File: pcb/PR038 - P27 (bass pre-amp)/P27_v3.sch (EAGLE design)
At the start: 51 parts, among them IC1 NE5532P, Q1 BC337

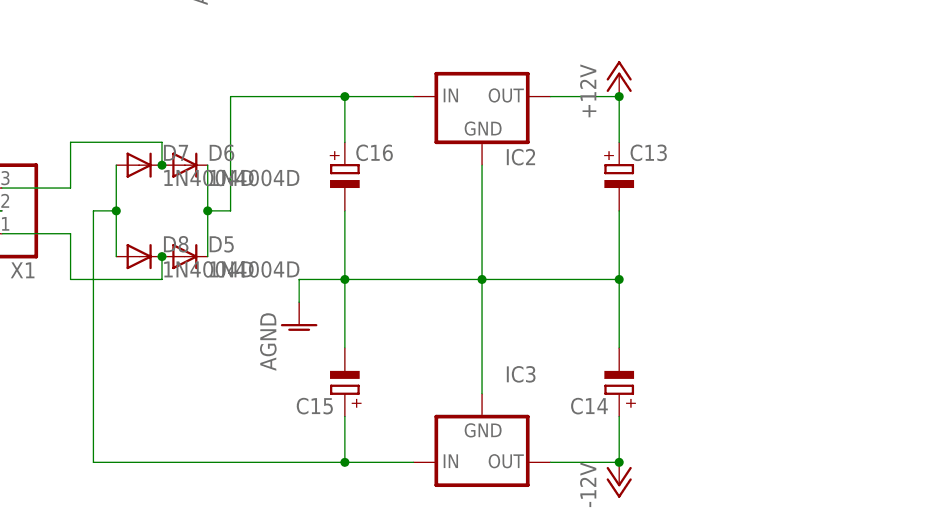
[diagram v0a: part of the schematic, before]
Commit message: 
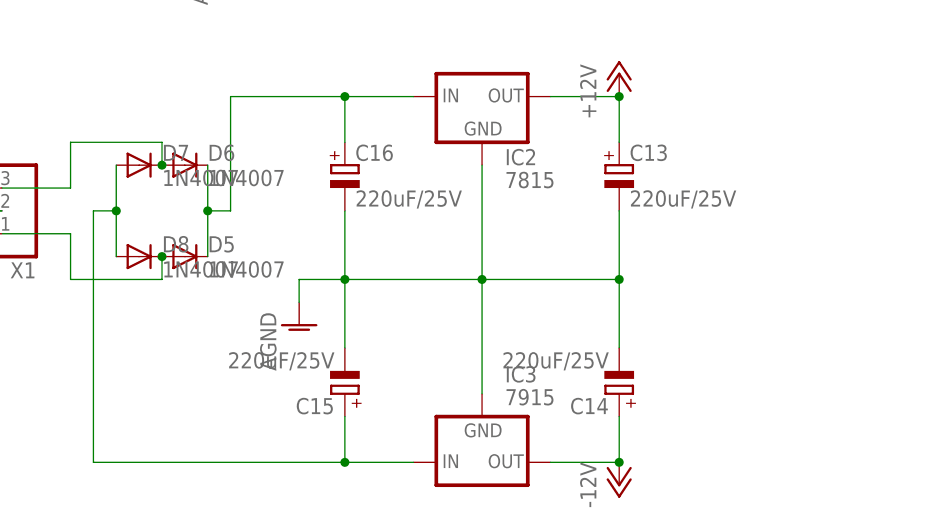
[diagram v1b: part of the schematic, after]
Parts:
- C13, C14, C15, C16: value (none) -> 220uF/25V
- D5, D6, D7, D8: value 1N4004D -> 1N4007
- IC2: value (none) -> 7815
- IC3: value (none) -> 7915
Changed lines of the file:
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@@
 <?xml version="1.0" encoding="utf-8"?>
 <!DOCTYPE eagle SYSTEM "eagle.dtd">
-<eagle version="6.4">
+<eagle version="6.5.0">
 <drawing>
 <settings>
@@
 <part name="X1" library="P27" deviceset="W237-103" device=""/>
 <part name="AGND10" library="P27" deviceset="AGND" device=""/>
-<part name="IC2" library="P27" deviceset="78XX" device="TO-220"/>
-<part name="C13" library="P27" deviceset="CPOL-EU" device="E2.5-6"/>
-<part name="C14" library="P27" deviceset="CPOL-EU" device="E2.5-6"/>
-<part name="C15" library="P27" deviceset="CPOL-EU" device="E2.5-6"/>
-<part name="C16" library="P27" deviceset="CPOL-EU" device="E2.5-6"/>
+<part name="IC2" library="P27" deviceset="78XX" device="TO-220" value="7815"/>
+<part name="C13" library="P27" deviceset="CPOL-EU" device="E2.5-6" value="220uF/25V"/>
+<part name="C14" library="P27" deviceset="CPOL-EU" device="E2.5-6" value="220uF/25V"/>
+<part name="C15" library="P27" deviceset="CPOL-EU" device="E2.5-6" value="220uF/25V"/>
+<part name="C16" library="P27" deviceset="CPOL-EU" device="E2.5-6" value="220uF/25V"/>
 <part name="AGND11" library="P27" deviceset="AGND" device=""/>
 <part name="P+3" library="P27" deviceset="+12V" device=""/>
 <part name="P-3" library="P27" deviceset="-12V" device=""/>
-<part name="IC3" library="P27" deviceset="79XX" device="TO-220"/>
+<part name="IC3" library="P27" deviceset="79XX" device="TO-220" value="7915"/>
 <part name="Q1" library="P27" deviceset="BC337" device=""/>
-<part name="D5" library="P27" deviceset="1N4004" device="D"/>
-<part name="D6" library="P27" deviceset="1N4004" device="D"/>
-<part name="D7" library="P27" deviceset="1N4004" device="D"/>
-<part name="D8" library="P27" deviceset="1N4004" device="D"/>
+<part name="D5" library="P27" deviceset="1N4004" device="D" value="1N4007"/>
+<part name="D6" library="P27" deviceset="1N4004" device="D" value="1N4007"/>
+<part name="D7" library="P27" deviceset="1N4004" device="D" value="1N4007"/>
+<part name="D8" library="P27" deviceset="1N4004" device="D" value="1N4007"/>
 </parts>
 <sheets>

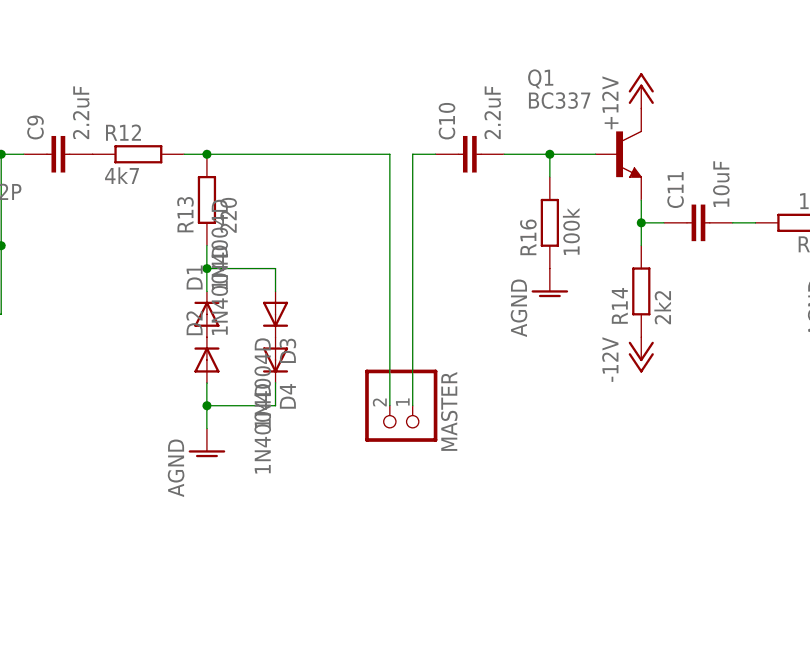
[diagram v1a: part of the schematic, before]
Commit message: 
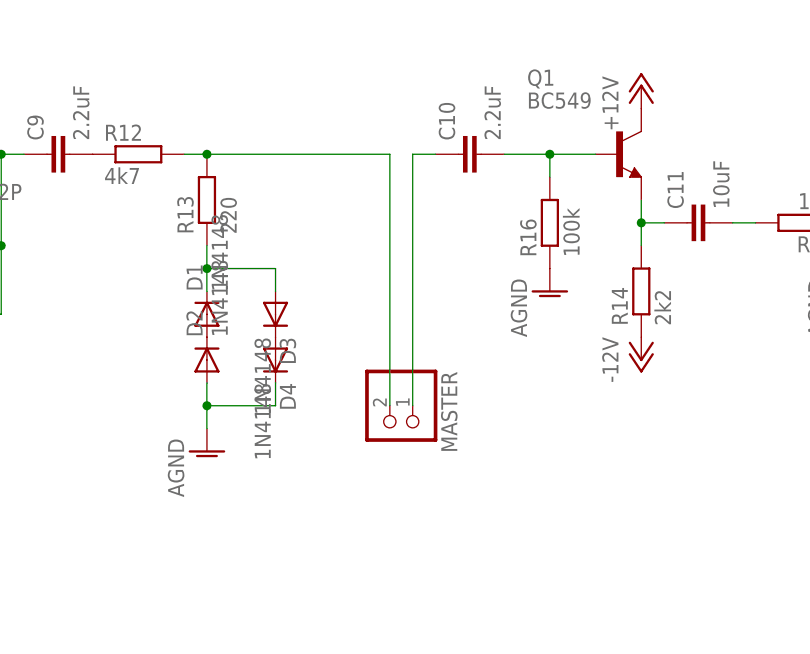
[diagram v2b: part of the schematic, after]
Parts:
- D1, D2, D3, D4: value 1N4004D -> 1N4148
- Q1: value BC337 -> BC549
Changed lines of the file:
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@@
 <part name="R12" library="P27" deviceset="R-EU_" device="0207/7" value="4k7"/>
 <part name="R13" library="P27" deviceset="R-EU_" device="0207/7" value="220"/>
-<part name="D1" library="P27" deviceset="1N4004" device="D"/>
-<part name="D2" library="P27" deviceset="1N4004" device="D"/>
-<part name="D3" library="P27" deviceset="1N4004" device="D"/>
-<part name="D4" library="P27" deviceset="1N4004" device="D"/>
+<part name="D1" library="P27" deviceset="1N4004" device="D" value="1N4148"/>
+<part name="D2" library="P27" deviceset="1N4004" device="D" value="1N4148"/>
+<part name="D3" library="P27" deviceset="1N4004" device="D" value="1N4148"/>
+<part name="D4" library="P27" deviceset="1N4004" device="D" value="1N4148"/>
 <part name="AGND4" library="P27" deviceset="AGND" device=""/>
 <part name="AGND5" library="P27" deviceset="AGND" device=""/>
@@
 <part name="P-3" library="P27" deviceset="-12V" device=""/>
 <part name="IC3" library="P27" deviceset="79XX" device="TO-220" value="7915"/>
-<part name="Q1" library="P27" deviceset="BC337" device=""/>
+<part name="Q1" library="P27" deviceset="BC337" device="" value="BC549"/>
 <part name="D5" library="P27" deviceset="1N4004" device="D" value="1N4007"/>
 <part name="D6" library="P27" deviceset="1N4004" device="D" value="1N4007"/>

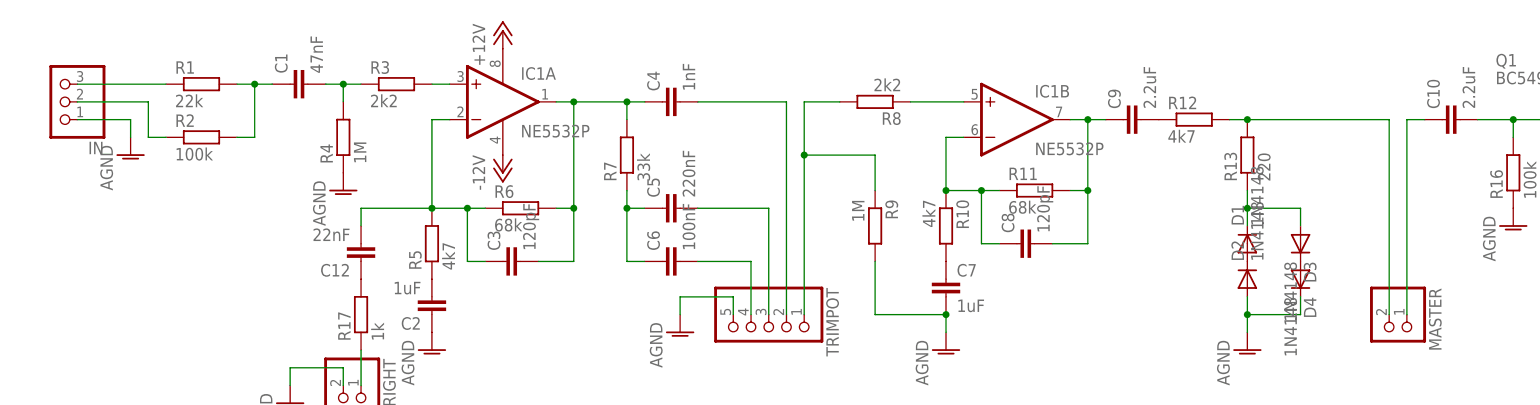
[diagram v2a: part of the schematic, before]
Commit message: 
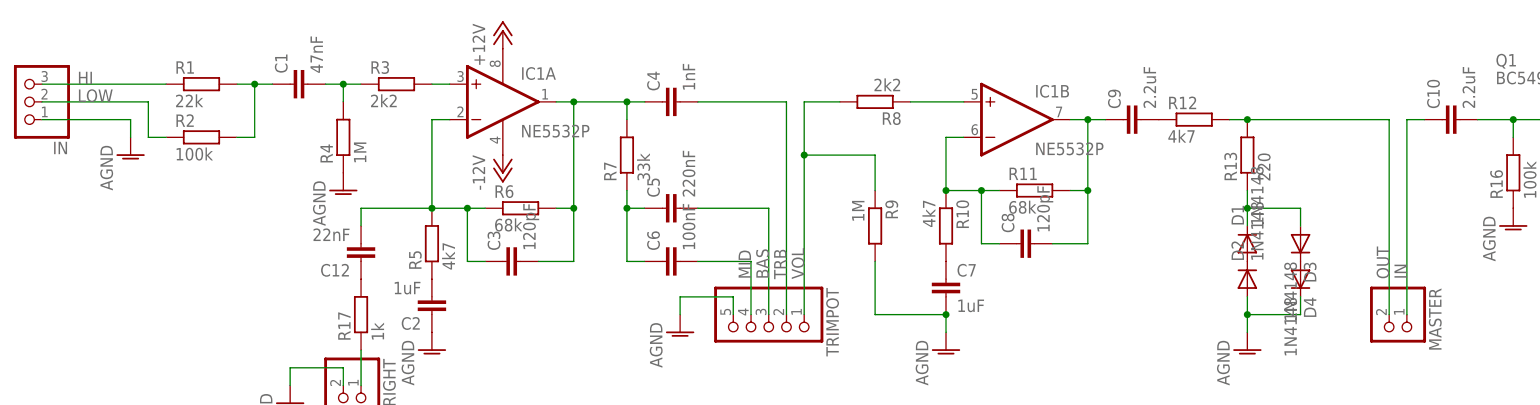
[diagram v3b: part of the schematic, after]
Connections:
- net N$10 renamed TRB
- net N$13 renamed VOL
- net N$21 renamed OUT
- net N$25 renamed HI
- net N$26 renamed LOW
- net N$27 renamed IN
- net N$7 renamed MID
- net N$9 renamed BAS
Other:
- moved on the sheet: IN
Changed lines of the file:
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@@
 <?xml version="1.0" encoding="utf-8"?>
 <!DOCTYPE eagle SYSTEM "eagle.dtd">
-<eagle version="6.5.0">
+<eagle version="7.1.0">
 <drawing>
 <settings>
@@
 <instance part="OUT" gate="G$1" x="236.22" y="22.86"/>
 <instance part="AGND7" gate="VR1" x="228.6" y="17.78"/>
-<instance part="IN" gate="A" x="-12.7" y="35.56" rot="R180"/>
+<instance part="IN" gate="A" x="-17.78" y="35.56" rot="R180"/>
 <instance part="AGND8" gate="VR1" x="-2.54" y="27.94"/>
 <instance part="C12" gate="G$1" x="30.48" y="12.7" rot="R180"/>
@@
 <segment>
 <pinref part="IN" gate="A" pin="1"/>
-<wire x1="-10.16" y1="33.02" x2="-2.54" y2="33.02" width="0.1524" layer="91"/>
+<wire x1="-15.24" y1="33.02" x2="-2.54" y2="33.02" width="0.1524" layer="91"/>
 <pinref part="AGND8" gate="VR1" pin="AGND"/>
 <wire x1="-2.54" y1="33.02" x2="-2.54" y2="30.48" width="0.1524" layer="91"/>
@@
 </segment>
 </net>
-<net name="N$7" class="0">
+<net name="MID" class="0">
 <segment>
 <pinref part="C6" gate="G$1" pin="2"/>
@@
 <wire x1="78.74" y1="12.7" x2="86.36" y2="12.7" width="0.1524" layer="91"/>
 <wire x1="86.36" y1="12.7" x2="86.36" y2="5.08" width="0.1524" layer="91"/>
-</segment>
-</net>
-<net name="N$9" class="0">
+<label x="86.36" y="10.16" size="1.778" layer="95" rot="R90"/>
+</segment>
+</net>
+<net name="BAS" class="0">
 <segment>
 <pinref part="C5" gate="G$1" pin="2"/>
@@
 <wire x1="78.74" y1="20.32" x2="88.9" y2="20.32" width="0.1524" layer="91"/>
 <wire x1="88.9" y1="20.32" x2="88.9" y2="5.08" width="0.1524" layer="91"/>
-</segment>
-</net>
-<net name="N$10" class="0">
+<label x="88.9" y="10.16" size="1.778" layer="95" rot="R90"/>
+</segment>
+</net>
+<net name="TRB" class="0">
 <segment>
 <pinref part="C4" gate="G$1" pin="2"/>
@@
 <wire x1="78.74" y1="35.56" x2="91.44" y2="35.56" width="0.1524" layer="91"/>
 <wire x1="91.44" y1="35.56" x2="91.44" y2="5.08" width="0.1524" layer="91"/>
+<label x="91.44" y="10.16" size="1.778" layer="95" rot="R90"/>
 </segment>
 </net>
@@
 </segment>
 </net>
-<net name="N$13" class="0">
+<net name="VOL" class="0">
 <segment>
 <pinref part="TRIMPOT" gate="A" pin="1"/>
@@
 <wire x1="104.14" y1="27.94" x2="93.98" y2="27.94" width="0.1524" layer="91"/>
 <junction x="93.98" y="27.94"/>
+<label x="93.98" y="10.16" size="1.778" layer="95" rot="R90"/>
 </segment>
 </net>
@@
 </segment>
 </net>
-<net name="N$21" class="0">
+<net name="OUT" class="0">
 <segment>
 <pinref part="R12" gate="G$1" pin="2"/>
@@
 <wire x1="177.8" y1="33.02" x2="177.8" y2="5.08" width="0.1524" layer="91"/>
 <junction x="157.48" y="33.02"/>
+<label x="177.8" y="10.16" size="1.778" layer="95" rot="R90"/>
 </segment>
 </net>
@@
 </segment>
 </net>
-<net name="N$27" class="0">
+<net name="IN" class="0">
 <segment>
 <pinref part="MASTER" gate="G$1" pin="1"/>
@@
 <wire x1="180.34" y1="33.02" x2="182.88" y2="33.02" width="0.1524" layer="91"/>
 <pinref part="C10" gate="G$1" pin="1"/>
+<label x="180.34" y="10.16" size="1.778" layer="95" rot="R90"/>
 </segment>
 </net>
@@
 </segment>
 </net>
-<net name="N$25" class="0">
+<net name="HI" class="0">
 <segment>
 <pinref part="IN" gate="A" pin="3"/>
 <pinref part="R1" gate="G$1" pin="1"/>
-<wire x1="-10.16" y1="38.1" x2="2.54" y2="38.1" width="0.1524" layer="91"/>
-</segment>
-</net>
-<net name="N$26" class="0">
+<wire x1="-15.24" y1="38.1" x2="2.54" y2="38.1" width="0.1524" layer="91"/>
+<label x="-10.16" y="38.1" size="1.778" layer="95"/>
+</segment>
+</net>
+<net name="LOW" class="0">
 <segment>
 <pinref part="IN" gate="A" pin="2"/>
-<wire x1="-10.16" y1="35.56" x2="0" y2="35.56" width="0.1524" layer="91"/>
+<wire x1="-15.24" y1="35.56" x2="0" y2="35.56" width="0.1524" layer="91"/>
 <wire x1="0" y1="35.56" x2="0" y2="30.48" width="0.1524" layer="91"/>
 <pinref part="R2" gate="G$1" pin="1"/>
 <wire x1="0" y1="30.48" x2="2.54" y2="30.48" width="0.1524" layer="91"/>
-</segment>
-</net>
+<label x="-10.16" y="35.56" size="1.778" layer="95"/>
+</segment>
+</net>
